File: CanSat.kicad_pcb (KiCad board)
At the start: 2 copper layers, 55.1 x 54.9 mm, 0 parts

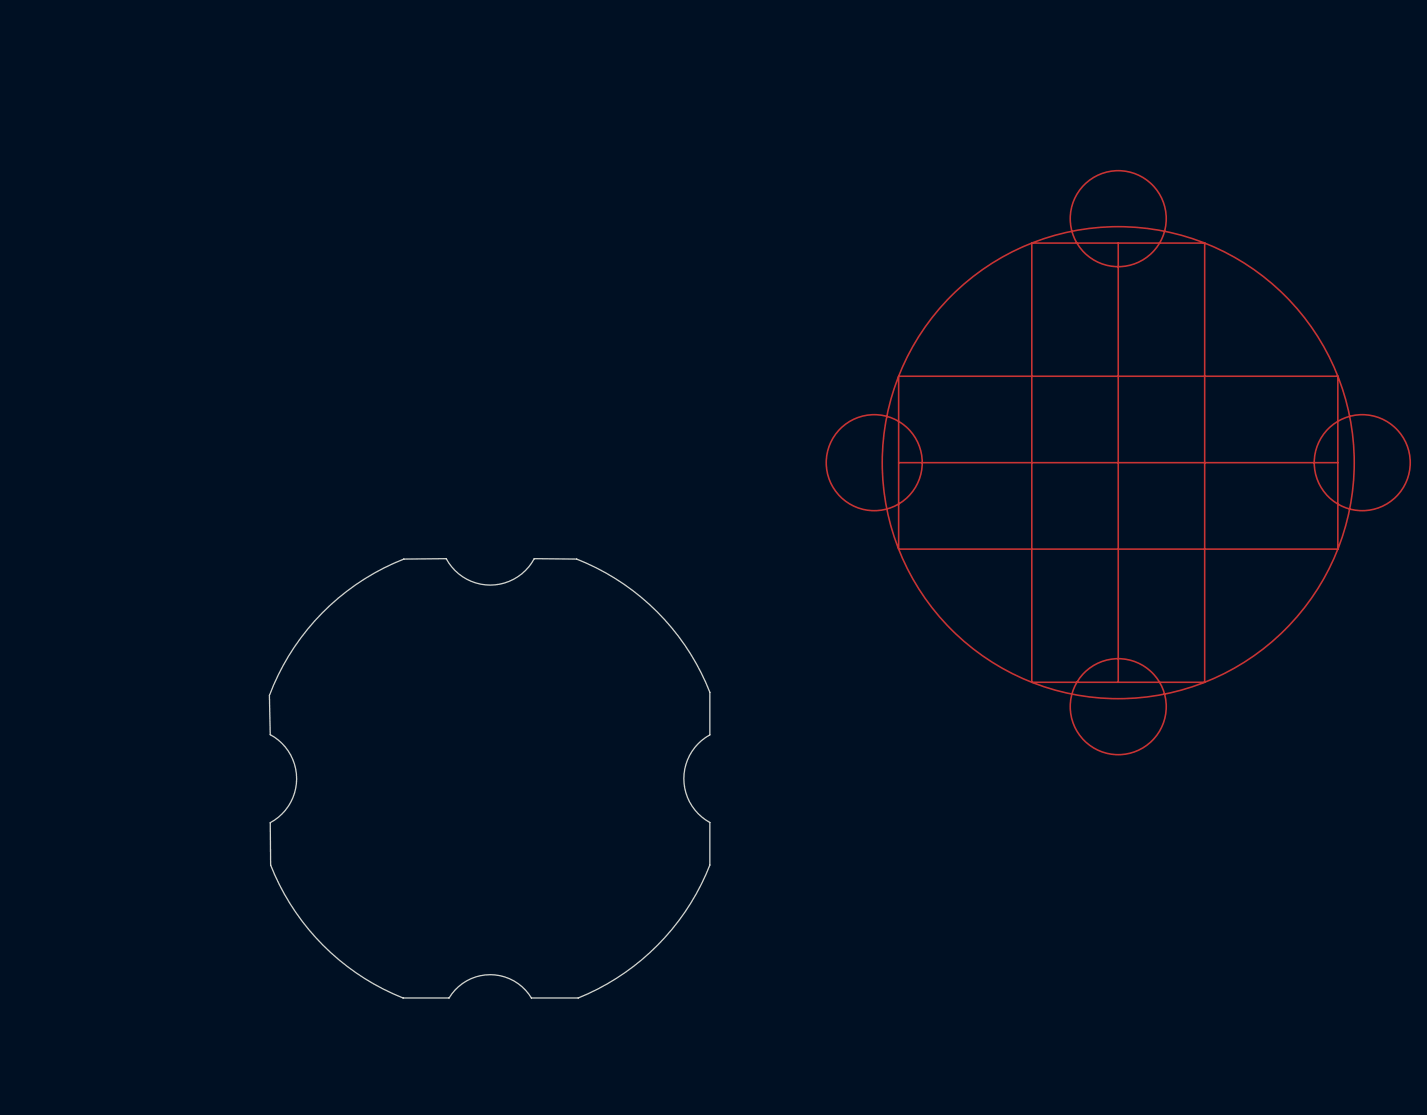
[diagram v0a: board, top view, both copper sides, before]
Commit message: Add components to pcb
Added:
3V3 power source
USB-C connector
Flash memory and PSRAM
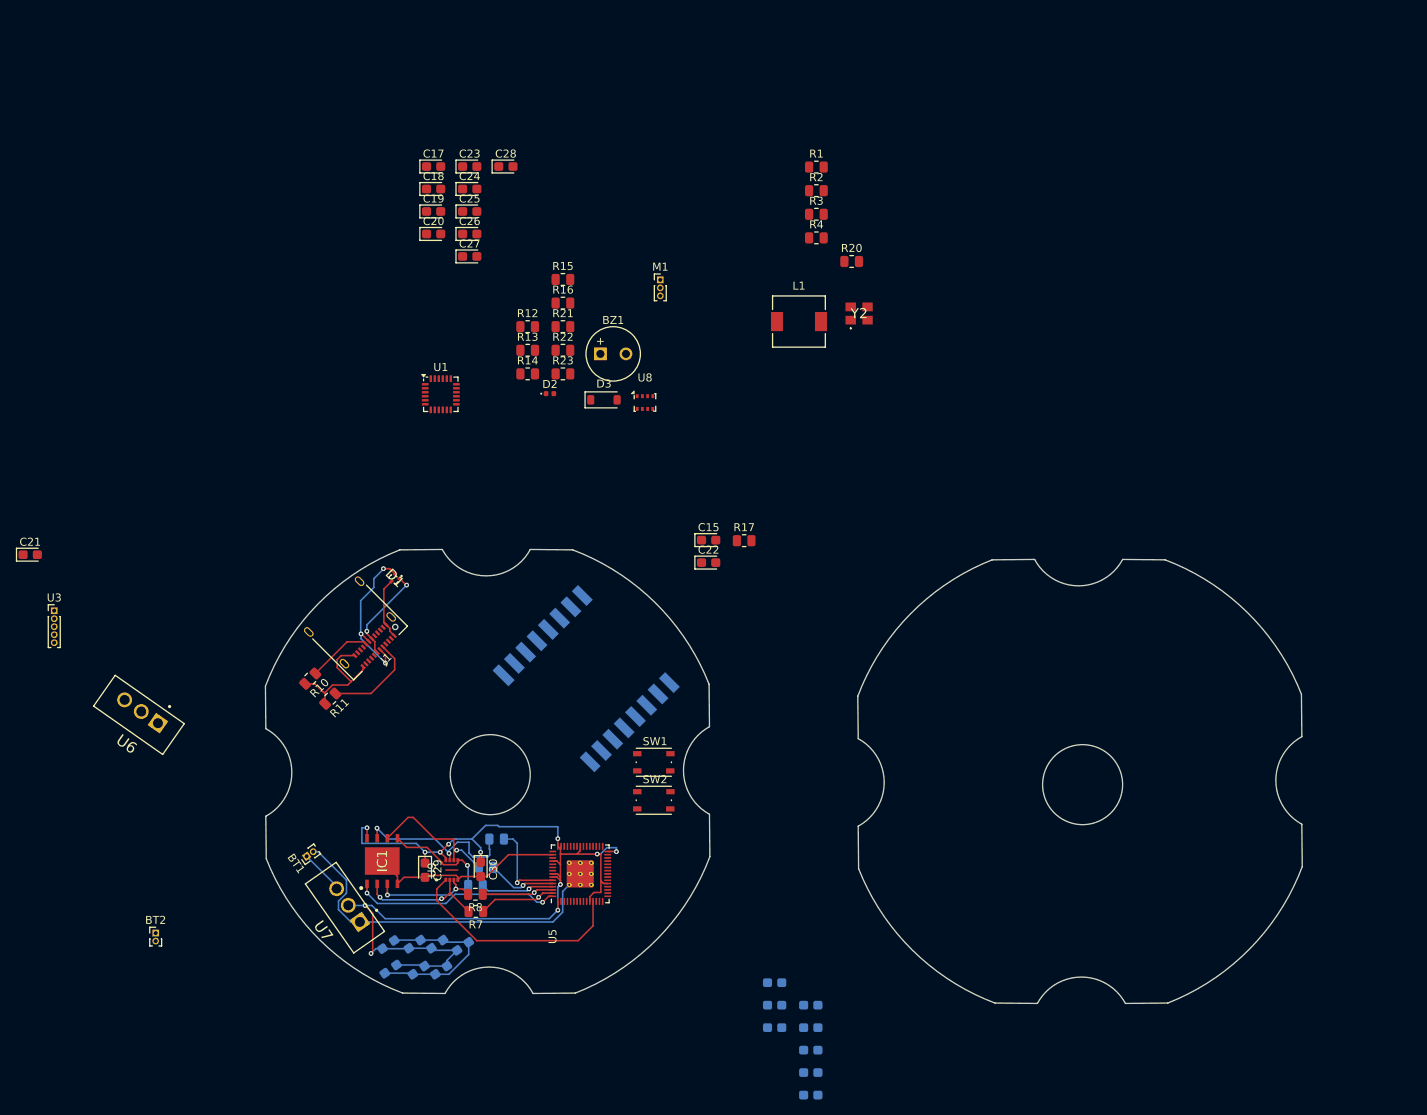
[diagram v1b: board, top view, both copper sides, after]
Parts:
- added BT1: Battery, Connector_PinHeader_1.00mm:PinHeader_1x02_P1.00mm_Vertical, F.Cu at (49.0, 141.7)
- added BT2: Battery, Connector_PinHeader_1.00mm:PinHeader_1x02_P1.00mm_Vertical, F.Cu at (30.2, 151.3)
- added BZ1: Buzzer, Buzzer_Beeper:MagneticBuzzer_Kingstate_KCG0601, F.Cu at (85.8, 78.9)
- added C1: 100nF, Capacitor_Tantalum_SMD:CP_EIA-2012-15_AVX-P, B.Cu at (59.5, 155.8)
- added C10: 100nF, Capacitor_Tantalum_SMD:CP_EIA-2012-15_AVX-P, B.Cu at (112.1, 165.9)
- added C11: 4.7uF, Capacitor_Tantalum_SMD:CP_EIA-2012-15_AVX-P, B.Cu at (112.1, 168.7)
- added C12: 100nF, Capacitor_Tantalum_SMD:CP_EIA-2012-15_AVX-P, B.Cu at (112.1, 171.6)
- added C13: 1uF, Capacitor_Tantalum_SMD:CP_EIA-2012-15_AVX-P, B.Cu at (107.5, 157.5)
- added C14: 1uF, Capacitor_Tantalum_SMD:CP_EIA-2012-15_AVX-P, B.Cu at (107.5, 160.3)
- added C15: 100nF, Capacitor_Tantalum_SMD:CP_EIA-2012-15_AVX-P, F.Cu at (99.3, 102.2)
- added C16: 4.7uF, Capacitor_Tantalum_SMD:CP_EIA-2012-15_AVX-P, B.Cu at (107.5, 163.1)
- added C17: 0.1uF, Capacitor_Tantalum_SMD:CP_EIA-2012-15_AVX-P, F.Cu at (64.9, 55.5)
- added C18: 2.2nF, Capacitor_Tantalum_SMD:CP_EIA-2012-15_AVX-P, F.Cu at (64.9, 58.3)
- added C19: 2.2nF, Capacitor_Tantalum_SMD:CP_EIA-2012-15_AVX-P, F.Cu at (64.9, 61.1)
- added C2: 100nF, Capacitor_Tantalum_SMD:CP_EIA-2012-15_AVX-P, B.Cu at (63.0, 155.9)
- added C20: 1uF, Capacitor_Tantalum_SMD:CP_EIA-2012-15_AVX-P, F.Cu at (64.9, 63.9)
- added C21: 1uF, Capacitor_Tantalum_SMD:CP_EIA-2012-15_AVX-P, F.Cu at (14.5, 104.0)
- added C22: 100nF, Capacitor_Tantalum_SMD:CP_EIA-2012-15_AVX-P, F.Cu at (99.3, 105.0)
- added C23: 10µf, Capacitor_Tantalum_SMD:CP_EIA-2012-15_AVX-P, F.Cu at (69.4, 55.5)
- added C24: 10uf, Capacitor_Tantalum_SMD:CP_EIA-2012-15_AVX-P, F.Cu at (69.4, 58.3)
- added C25: 10µf, Capacitor_Tantalum_SMD:CP_EIA-2012-15_AVX-P, F.Cu at (69.4, 61.1)
- added C26: 10uf, Capacitor_Tantalum_SMD:CP_EIA-2012-15_AVX-P, F.Cu at (69.4, 63.9)
- added C27: 100nF, Capacitor_Tantalum_SMD:CP_EIA-2012-15_AVX-P, F.Cu at (69.4, 66.7)
- added C28: 100nF, Capacitor_Tantalum_SMD:CP_EIA-2012-15_AVX-P, F.Cu at (74.0, 55.5)
- added C29: 2.2uF, Capacitor_Tantalum_SMD:CP_EIA-2012-15_AVX-P, F.Cu at (63.9, 143.4)
- added C3: 100nF, Capacitor_Tantalum_SMD:CP_EIA-2012-15_AVX-P, B.Cu at (65.9, 155.9)
- added C30: 100nF, Capacitor_Tantalum_SMD:CP_EIA-2012-15_AVX-P, F.Cu at (70.8, 143.3)
- added C4: 100nF, Capacitor_Tantalum_SMD:CP_EIA-2012-15_AVX-P, B.Cu at (59.3, 152.7)
- added C5: 100nF, Capacitor_Tantalum_SMD:CP_EIA-2012-15_AVX-P, B.Cu at (62.6, 152.7)
- added C6: 100nF, Capacitor_Tantalum_SMD:CP_EIA-2012-15_AVX-P, B.Cu at (65.4, 152.7)
- added C7: 100nF, Capacitor_Tantalum_SMD:CP_EIA-2012-15_AVX-P, B.Cu at (68.6, 152.9)
- added C8: 4.7uF, Capacitor_Tantalum_SMD:CP_EIA-2012-15_AVX-P, B.Cu at (112.1, 160.3)
- added C9: 4.7uF, Capacitor_Tantalum_SMD:CP_EIA-2012-15_AVX-P, B.Cu at (112.1, 163.1)
- added D1: ESD7L5.0DT5G, SamacSys_Parts:MMBT2907AM3T5G, F.Cu at (60.0, 107.0)
- added D2: LED, LED_SMD:LED_0402_1005Metric, F.Cu at (79.5, 83.9)
- added D3: MBR0530, Diode_SMD:D_SOD-123, F.Cu at (86.2, 84.7)
- added IC1: W25Q128JVPIQ, SamacSys_Parts:SON127P600X500X80-9N-D, F.Cu at (58.5, 142.3)
- added J1: USB_C_Receptacle, Connector_USB:USB_C_Receptacle_Amphenol_12401610E4-2A, F.Cu at (54.5, 112.5)
- added L1: 3.3u, Inductor_SMD:L_6.3x6.3_H3, F.Cu at (110.6, 74.9)
- added M1: SG-90, Connector_PinHeader_1.00mm:PinHeader_1x03_P1.00mm_Vertical, F.Cu at (93.3, 69.7)
- added R1: 10K, Resistor_SMD:R_0805_2012Metric, F.Cu at (112.8, 55.5)
- added R10: 5.1K, Resistor_SMD:R_0805_2012Metric, F.Cu at (49.5, 119.5)
- added R11: 5.1K, Resistor_SMD:R_0805_2012Metric, F.Cu at (52.0, 122.0)
- added R12: 10K, Resistor_SMD:R_0805_2012Metric, F.Cu at (76.7, 75.5)
- added R13: 1K, Resistor_SMD:R_0805_2012Metric, F.Cu at (76.7, 78.5)
- added R14: 1K, Resistor_SMD:R_0805_2012Metric, F.Cu at (76.7, 81.4)
- added R15: 10K, Resistor_SMD:R_0805_2012Metric, F.Cu at (81.1, 69.6)
- added R16: DNC, Resistor_SMD:R_0805_2012Metric, F.Cu at (81.1, 72.5)
- added R17: 100R, Resistor_SMD:R_0805_2012Metric, F.Cu at (103.7, 102.2)
- added R2: 10K, Resistor_SMD:R_0805_2012Metric, F.Cu at (112.8, 58.5)
- added R20: 33, Resistor_SMD:R_0805_2012Metric, F.Cu at (117.2, 67.3)
- added R21: 10K, Resistor_SMD:R_0805_2012Metric, F.Cu at (81.1, 75.5)
- added R22: 10K, Resistor_SMD:R_0805_2012Metric, F.Cu at (81.1, 78.5)
- added R23: 10K, Resistor_SMD:R_0805_2012Metric, F.Cu at (81.1, 81.4)
- added R3: 27, Resistor_SMD:R_0805_2012Metric, F.Cu at (112.8, 61.5)
- added R4: 27, Resistor_SMD:R_0805_2012Metric, F.Cu at (112.8, 64.4)
- added R5: 27, Resistor_SMD:R_0805_2012Metric, B.Cu at (71.5, 143.1)
- added R6: 27, Resistor_SMD:R_0805_2012Metric, B.Cu at (70.2, 145.3)
- added R7: 27, Resistor_SMD:R_0805_2012Metric, F.Cu at (70.2, 148.6)
- added R8: 27, Resistor_SMD:R_0805_2012Metric, F.Cu at (70.2, 146.4)
- added R9: 27, Resistor_SMD:R_0805_2012Metric, B.Cu at (72.8, 139.6)
- added SW1: SW_Push, Button_Switch_SMD:SW_Push_1P1T_NO_Vertical_Wuerth_434133025816, F.Cu at (92.5, 129.9)
- added SW2: SW_Push, Button_Switch_SMD:SW_Push_1P1T_NO_Vertical_Wuerth_434133025816, F.Cu at (92.5, 134.7)
- added U1: MPU-6050, Sensor_Motion:InvenSense_QFN-24_4x4mm_P0.5mm, F.Cu at (65.8, 84.0)
- added U2: RA-02_LORA, RA-02_LORA:MODULE_RA-02_LORA, B.Cu at (84.0, 119.5)
- added U3: ~, Connector_PinHeader_1.00mm:PinHeader_1x05_P1.00mm_Vertical, F.Cu at (17.5, 111.0)
- added U5: RP2350_60QFN, RP2040:RP2350-QFN-60-1EP_7x7_P0.4mm_EP3.4x3.4mm_ThermalVias, F.Cu at (83.2, 143.9)
- added U6: LM1085-5.0, LM1085IT-5.0:TO254P1054X470X1955-3, F.Cu at (28.4, 123.6)
- added U7: LM1085-3.3, LM1085IT-3.3:TO254P1054X470X1955-3, F.Cu at (54.3, 147.8)
- added U8: BMP280, Package_LGA:Bosch_LGA-8_2x2.5mm_P0.65mm_ClockwisePinNumbering, F.Cu at (91.3, 85.0)
- added U9: APS6404L-3SQR-ZR, APS6404L-3SQR-ZR:PSON50P200X300X50-9N, F.Cu at (67.2, 143.4)
- added Y2: ASE-12.000MHz-E-T, SamacSys_Parts:ASE12000MHzET, F.Cu at (118.1, 73.9)
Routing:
- net +3V3: track 0.00 -> 124.2 mm, vias 0 -> 12
- net GND: track 0.00 -> 116.3 mm
- net /~{PSRAM_CS}: track 0.00 -> 28.5 mm
- net /QSPI_CSN: track 0.00 -> 26.1 mm, vias 0 -> 2
- net /QSPI_SD3: track 0.00 -> 22.0 mm, vias 0 -> 2
- net /USB_D+: track 0.00 -> 19.3 mm, vias 0 -> 3
- net /QSPI_SCLK: track 0.00 -> 17.2 mm, vias 0 -> 1
- net /QSPI_SD1: track 0.00 -> 16.0 mm, vias 0 -> 2
- net /QSPI_SD0: track 0.00 -> 13.4 mm, vias 0 -> 1
- net /QSPI_SD2: track 0.00 -> 13.3 mm, vias 0 -> 2
- net /USB_D-: track 0.00 -> 12.3 mm, vias 0 -> 2
- net Net-(J1-CC1): track 0.00 -> 12.1 mm
- net Net-(U5-QSPI_SD3): track 0.00 -> 11.4 mm, vias 0 -> 1
- net Net-(U5-QSPI_SD1): track 0.00 -> 9.65 mm, vias 0 -> 1
- net Net-(U5-QSPI_SD0): track 0.00 -> 9.24 mm, vias 0 -> 1
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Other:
- board size 55.1 x 54.9 mm -> 129.6 x 56.7 mm

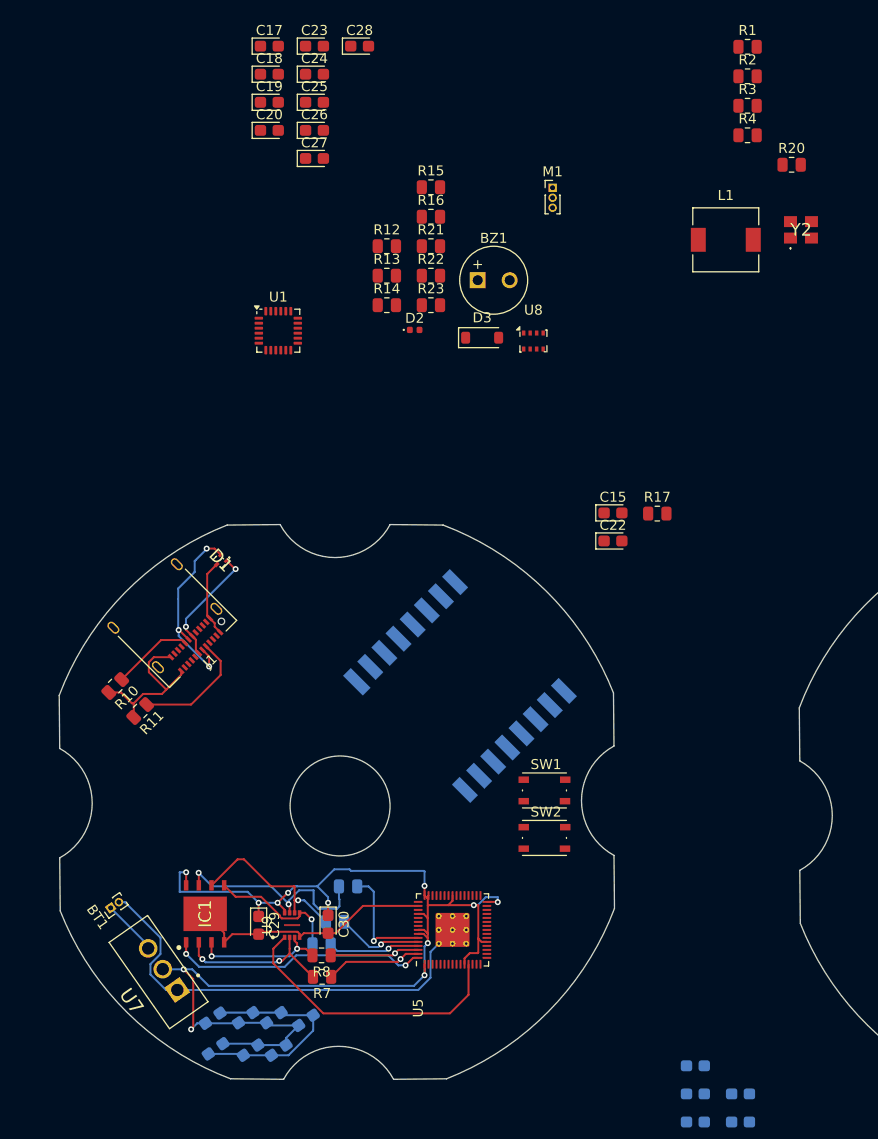
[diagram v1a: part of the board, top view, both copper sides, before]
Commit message: Connected LoRa
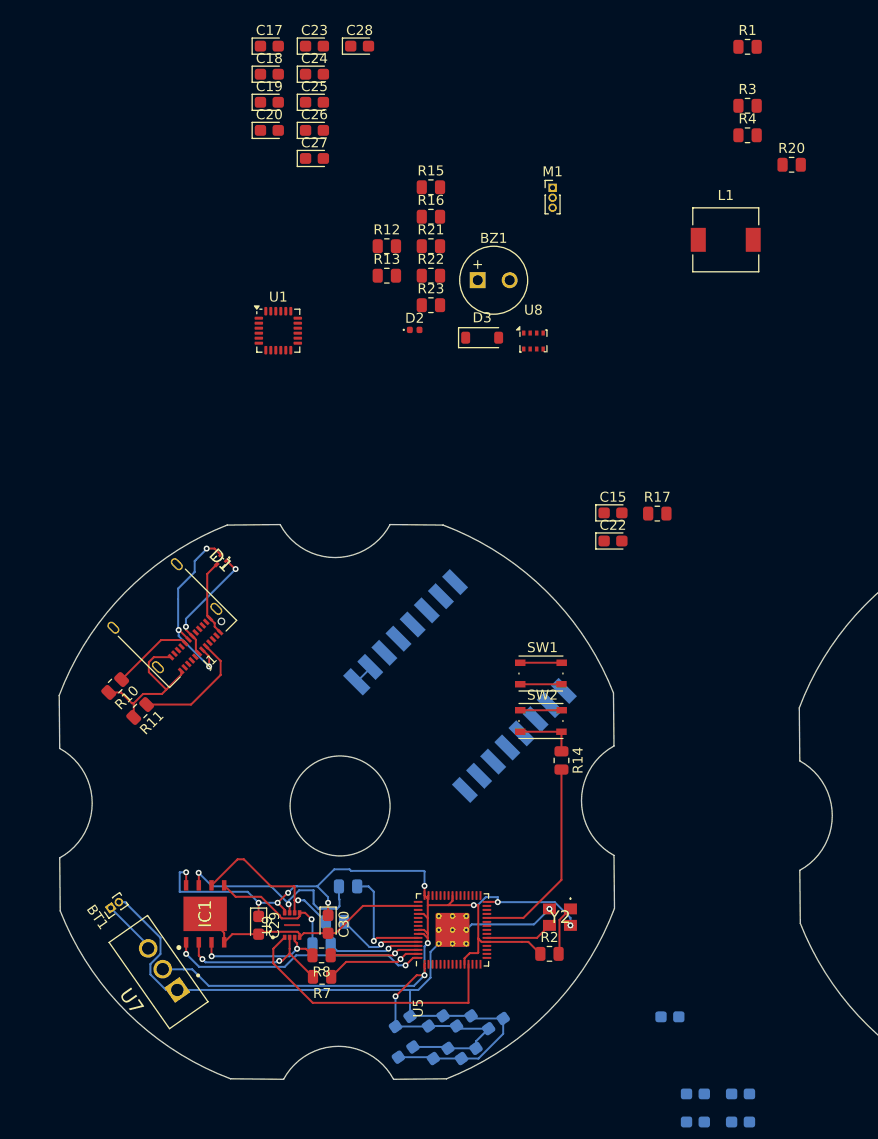
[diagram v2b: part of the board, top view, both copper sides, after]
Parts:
- moved R2 90.0 mm to (93.0, 146.3)
- moved Y2 72.9 mm to (94.0, 142.6), turned to 180 degrees
- moved R14 48.8 mm to (94.2, 127.0), turned to -90 degrees
- moved C1 19.0 mm to (78.6, 156.1)
- moved C2 19.0 mm to (82.1, 156.3)
- moved C4 19.0 mm to (78.3, 153.1)
- moved C3 19.0 mm to (84.9, 156.3)
- moved C5 19.0 mm to (81.6, 153.0)
- moved C6 19.0 mm to (84.4, 153.0)
- moved C7 19.0 mm to (87.6, 153.3)
- moved SW1 11.7 mm to (92.1, 118.2)
- moved SW2 11.7 mm to (92.1, 123.0)
- moved C13 5.52 mm to (105.0, 152.6)
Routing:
- net GND: track 116.3 -> 138.4 mm, vias 0 -> 1
- net /~{RST}: track 0.00 -> 20.1 mm
- net +3V3: track 124.2 -> 137.3 mm
- net /RP2350A/XIN: track 0.00 -> 6.78 mm
- net Net-(R14-Pad1): track 0.00 -> 6.09 mm
- net Net-(Y2-TRI-STATE_(STBY)): track 0.00 -> 4.99 mm
- net Net-(R13-Pad1): track 0.00 -> 4.12 mm

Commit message: Added more components to the pcb
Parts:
- C13: moved to F.Cu
- C19, C20, C22, C25, C26, R15, R16, U1: moved to B.Cu
- moved C24 96.7 mm to (57.3, 154.2), turned to 30 degrees
- moved C23 90.7 mm to (46.8, 143.3), turned to 90 degrees
- moved R3 89.8 mm to (74.3, 142.6), turned to 90 degrees
- moved R4 85.7 mm to (76.3, 141.9), turned to -90 degrees
- moved C17 84.5 mm to (54.5, 139.3), turned to -90 degrees
- moved R1 83.9 mm to (97.7, 138.1), turned to 90 degrees
- moved C18 83.6 mm to (45.4, 139.6), turned to -90 degrees
- moved R15 82.4 mm to (91.7, 151.3), turned to -135 degrees
- moved BZ1 79.1 mm to (61.7, 154.2)
- moved R16 76.8 mm to (93.0, 148.4)
- moved C28 73.1 mm to (47.5, 123.6), turned to -160 degrees
- moved C19 72.0 mm to (54.8, 132.4), turned to -45 degrees
- moved D2 66.4 mm to (86.3, 149.9), turned to 180 degrees
- moved L1 65.7 mm to (84.7, 135.2), turned to 180 degrees
- moved C27 62.5 mm to (48.3, 125.5), turned to -160 degrees
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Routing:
- net GND: track 138.4 -> 318.8 mm, vias 1 -> 14
- net +3V3: track 137.3 -> 222.6 mm, vias 12 -> 17
- net /I2C0_SDA: track 0.00 -> 65.9 mm, vias 0 -> 4
- net /I2C0_SCL: track 0.00 -> 65.4 mm, vias 0 -> 4
- net /INT: track 0.00 -> 45.5 mm, vias 0 -> 3
- net /RADIO_RX_TIMEOUT: track 0.00 -> 43.5 mm
- net /USB_D+: track 19.3 -> 62.0 mm, vias 3 -> 5
- net /USB_D-: track 12.3 -> 55.0 mm, vias 2 -> 4
- net /~{RST}: track 20.1 -> 61.4 mm, vias 0 -> 1
- net /SERVO: track 0.00 -> 40.8 mm, vias 0 -> 2
- net /GPS_RX: track 0.00 -> 38.7 mm, vias 0 -> 2
- net /BUZZER: track 0.00 -> 38.0 mm
- net /GPS_TX: track 0.00 -> 36.0 mm, vias 0 -> 2
- net /RADIO_RX_INT: track 0.00 -> 24.3 mm, vias 0 -> 2
- net /SPI0_RX: track 0.00 -> 21.5 mm, vias 0 -> 1
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
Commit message: Connected all components
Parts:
- C9: moved to F.Cu
- D3, R13: moved to B.Cu
- moved C16 87.4 mm to (168.6, 100.6), turned to 0 degrees
- moved C12 86.3 mm to (168.8, 106.5), turned to 0 degrees
- moved C11 85.6 mm to (168.7, 104.5), turned to 0 degrees
- moved C10 85.0 mm to (168.7, 102.5), turned to 0 degrees
- moved C6 82.3 mm to (160.8, 122.7)
- moved C14 82.1 mm to (173.6, 111.4), turned to 90 degrees
- moved J1 82.1 mm to (130.8, 82.2)
- moved C7 82.0 mm to (163.7, 122.9)
- moved C13 82.0 mm to (171.5, 107.7)
- moved C18 82.0 mm to (121.5, 109.2)
- moved C19 82.0 mm to (130.9, 102.0)
- moved C20 82.0 mm to (145.5, 83.5)
- moved C22 82.0 mm to (150.8, 83.8)
- moved C23 82.0 mm to (122.9, 112.9)
- moved C25 82.0 mm to (142.8, 77.3)
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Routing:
- net Net-(R13-Pad1): track 4.12 -> 56.2 mm, vias 0 -> 1
- net +1V1: track 7.15 -> 51.3 mm, vias 0 -> 9
- net GND: track 318.8 -> 359.6 mm, vias 14 -> 21
- net +3V3: track 222.6 -> 241.5 mm, vias 17 -> 21
- net /QSPI_CSN: track 26.1 -> 41.1 mm, vias 2 -> 3
- net /USER_SW: track 0.00 -> 11.9 mm, vias 0 -> 2
- net Net-(R22-Pad2): track 0.00 -> 11.2 mm, vias 0 -> 4
- net /RP2350A/VREG_AVDD: track 0.00 -> 9.94 mm, vias 0 -> 3
- net Net-(D3-K): track 0.00 -> 2.06 mm
- net Net-(U5-QSPI_SD1): vias 1 -> 0
- net Net-(U5-QSPI_SD2): vias 1 -> 0
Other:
- board size 129.6 x 56.7 mm -> 55.6 x 55.5 mm
